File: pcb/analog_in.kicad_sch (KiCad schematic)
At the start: 16 parts, among them J8 Guitar Input, J9 Guitar Output, U2 TL072

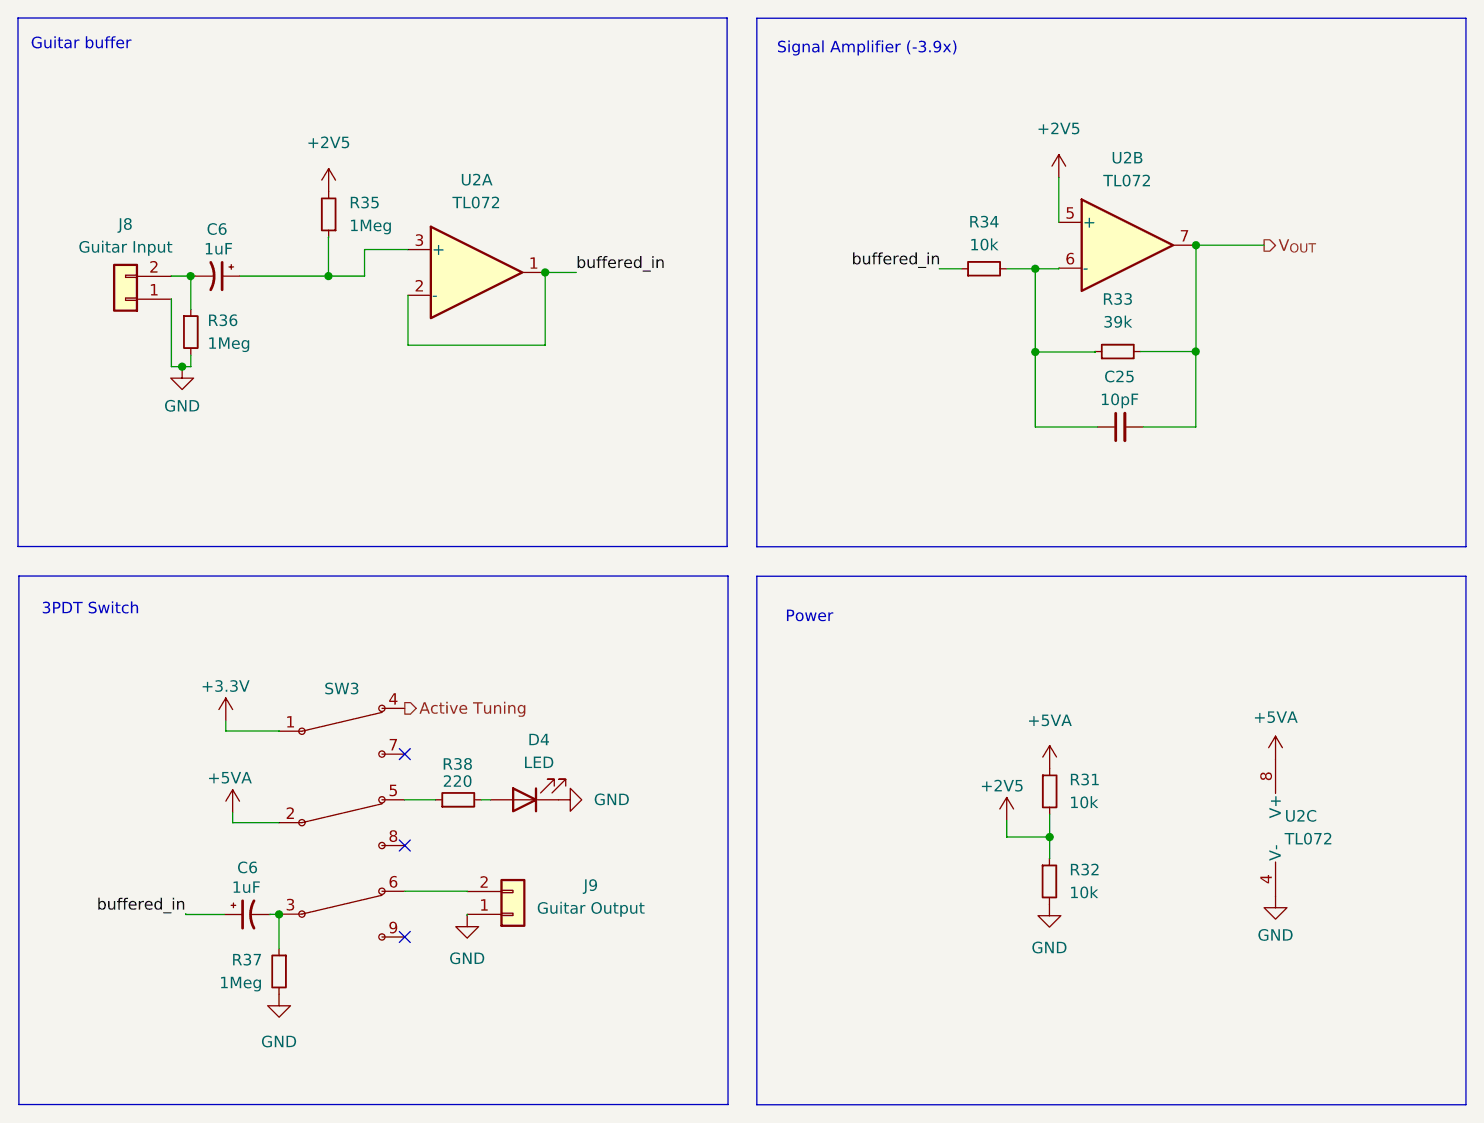
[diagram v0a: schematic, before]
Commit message: Reordered components
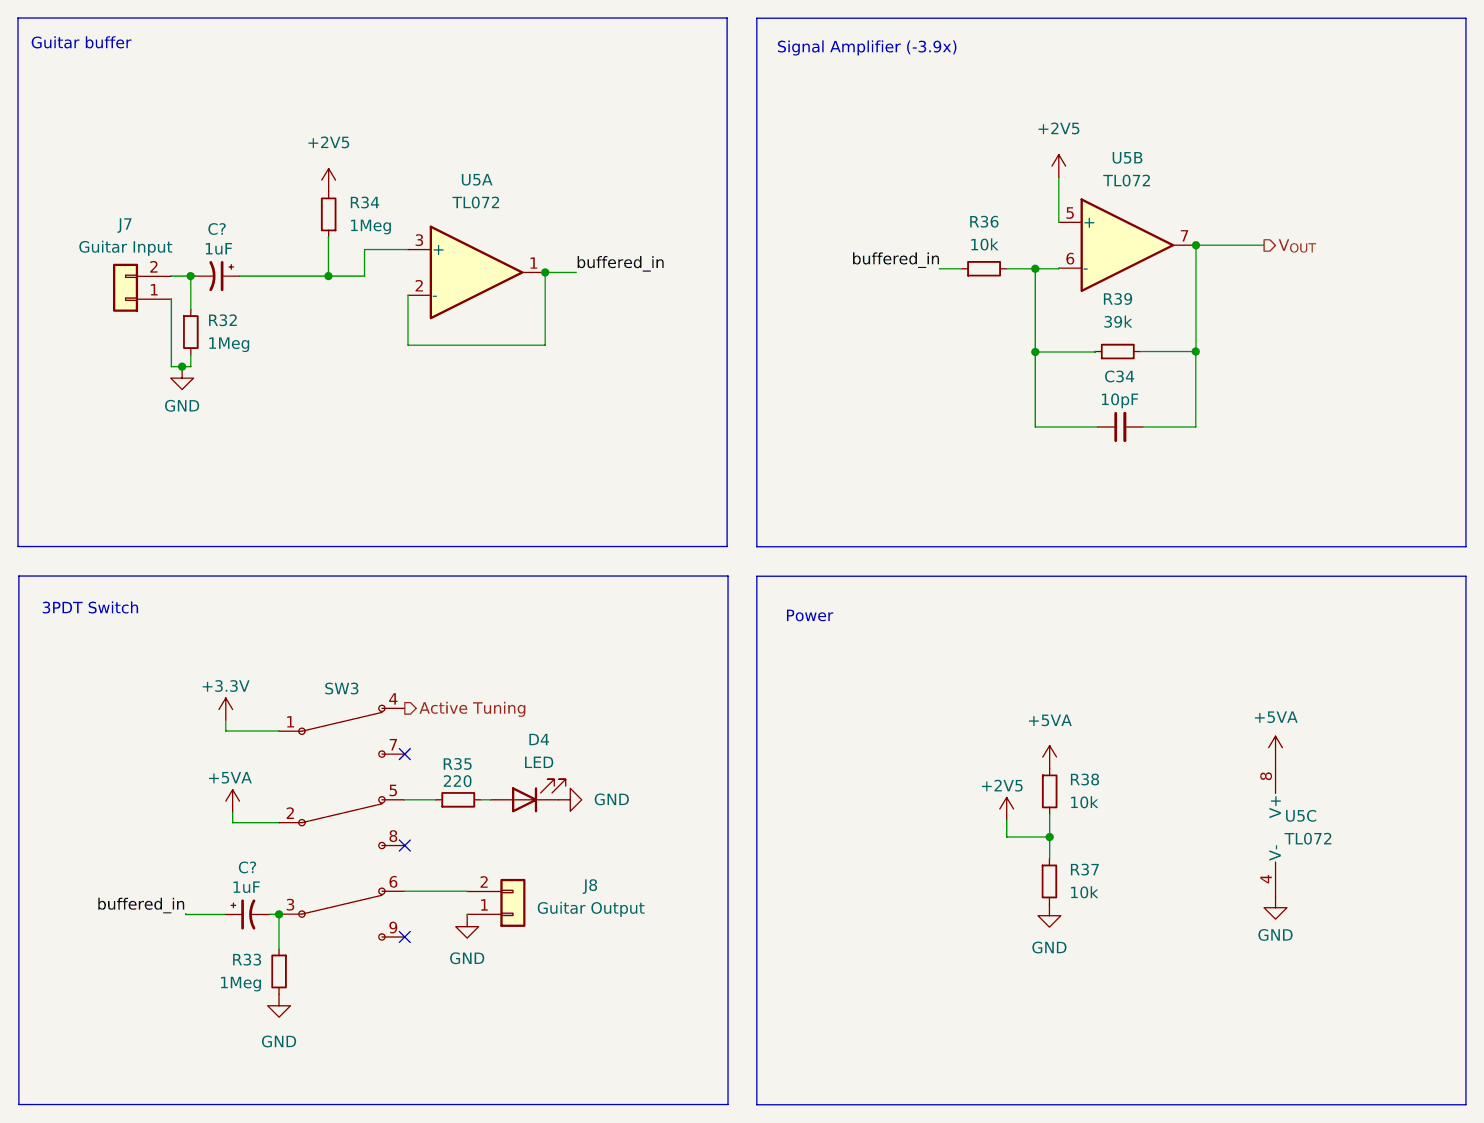
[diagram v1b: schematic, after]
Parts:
- renumbered C25 to C34, C6 to C?, J8 to J7, J9 to J8, R36 to R32, R37 to R33, R35 to R34, R38 to R35, R34 to R36, R32 to R37, R31 to R38, R33 to R39, U2 to U5
